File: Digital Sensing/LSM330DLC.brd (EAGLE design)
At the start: 7 parts

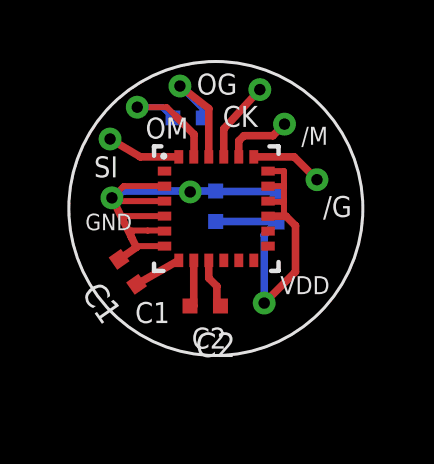
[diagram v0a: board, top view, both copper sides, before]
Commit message: minor modification on OSHW logo; added LSM330DLC reference design
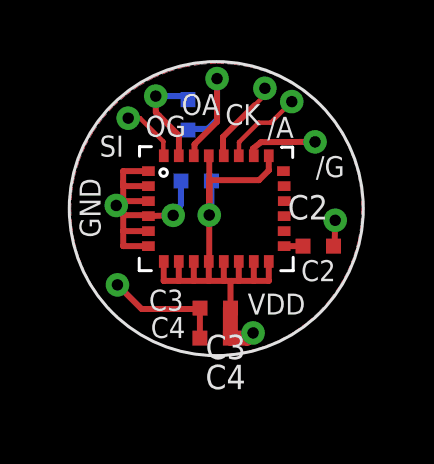
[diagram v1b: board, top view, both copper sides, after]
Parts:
- removed U$1: LSM9DS09DOFS0, lsm9ds0:LGA24(4X4X1)
- added IC1: LSM330DLC, LSM330DLC:LSM330DLC
- C1: value 4.7uF -> 100n
- C2: value 0.22uF -> 4.7u
- C3: value 10uF -> 100n
- C4: value 100nF -> 10u
- R1: value (none) -> 0
- moved C4 4.84 mm to (-0.04, -4.32), flipped to the top, turned to 180 degrees
- moved C2 4.26 mm to (3.40, -1.25), turned to 0 degrees
- moved C1 3.79 mm to (-0.67, 0.92), flipped to the bottom, turned to 0 degrees
- moved C3 3.40 mm to (-0.03, -3.32), flipped to the top, turned to 180 degrees
- moved R1 0.10 mm to (-0.94, 3.12), turned to 90 degrees
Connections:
- removed net CS_G: U$1.P$19
- removed net CS_XM: U$1.P$20
- removed net N$1: C1.1, U$1.P$7
- removed net N$2: C2.2, U$1.P$8
- removed net N$3: C2.1, U$1.P$9
- removed net SDI: U$1.P$24
- removed net SDO_G: R1.1, U$1.P$22
- removed net SDO_XM: R1.2, U$1.P$23
- removed net SPC: U$1.P$21
- new net /CSA: IC1.CSA
- new net /CSG: IC1.CSG
- new net N$5: C2.1, IC1.CAP
- new net SCLAG: IC1.SCLAG
- new net SDIAG: IC1.SDAAG
- new net SDOA: IC1.SDOA, R1.2
- new net SDOG: IC1.SDOG, R1.1
- net GND: now also C2.2, C3.2, C4.2, IC1.GND1, IC1.GND2, IC1.RES1, IC1.RES2, IC1.RES3, IC1.RES4; no longer C3.1, C4.1, U$1.P$2, U$1.P$3, U$1.P$4, U$1.P$5, U$1.P$6
- net VDD: now also C1.1, C3.1, C4.1, IC1.RES5, IC1.RES6, IC1.RES7, IC1.RES8, IC1.RES9, IC1.VDD1, IC1.VDD2, IC1.VDD3, IC1.VDDIO1, IC1.VDDIO2; no longer C3.2, C4.2, U$1.P$15, U$1.P$16, U$1.P$17, U$1.P$18
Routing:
- net VDD: track 13.2 -> 19.9 mm, vias 1 -> 2
- net SDOG: track 0.00 -> 5.38 mm, vias 0 -> 1
- net SDO_XM: track 4.36 -> 0.00 mm, vias 1 -> 0
- net SDO_G: track 4.21 -> 0.00 mm, vias 1 -> 0
- net SDOA: track 0.00 -> 3.44 mm, vias 0 -> 1
- net SCLAG: track 0.00 -> 2.82 mm, vias 0 -> 1
- net /CSA: track 0.00 -> 2.77 mm, vias 0 -> 1
- net SPC: track 2.71 -> 0.00 mm, vias 1 -> 0
- net SDI: track 2.45 -> 0.00 mm, vias 1 -> 0
- net CS_G: track 2.42 -> 0.00 mm, vias 1 -> 0
- net /CSG: track 0.00 -> 2.41 mm, vias 0 -> 1
- net CS_XM: track 2.29 -> 0.00 mm, vias 1 -> 0
- net SDIAG: track 0.00 -> 1.97 mm, vias 0 -> 1
- net N$3: track 1.75 -> 0.00 mm
- net N$2: track 1.65 -> 0.00 mm
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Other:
- board outline added: 5.1 x 4.1 mm
- board text added: "/A"
- board text added: "LSM330DLC"
- board text added: "OA"
- board text removed: "/M"
- board text removed: "LSM9DS0"
- board text removed: "OM"
